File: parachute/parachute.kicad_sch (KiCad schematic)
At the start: 10 parts, among them J1 HMI, J2 battery, J3 trigger, J4 servo, J6 step_up, U1 Optocoupler_DC_PhotoNPN_AKEC, U2 RP2040

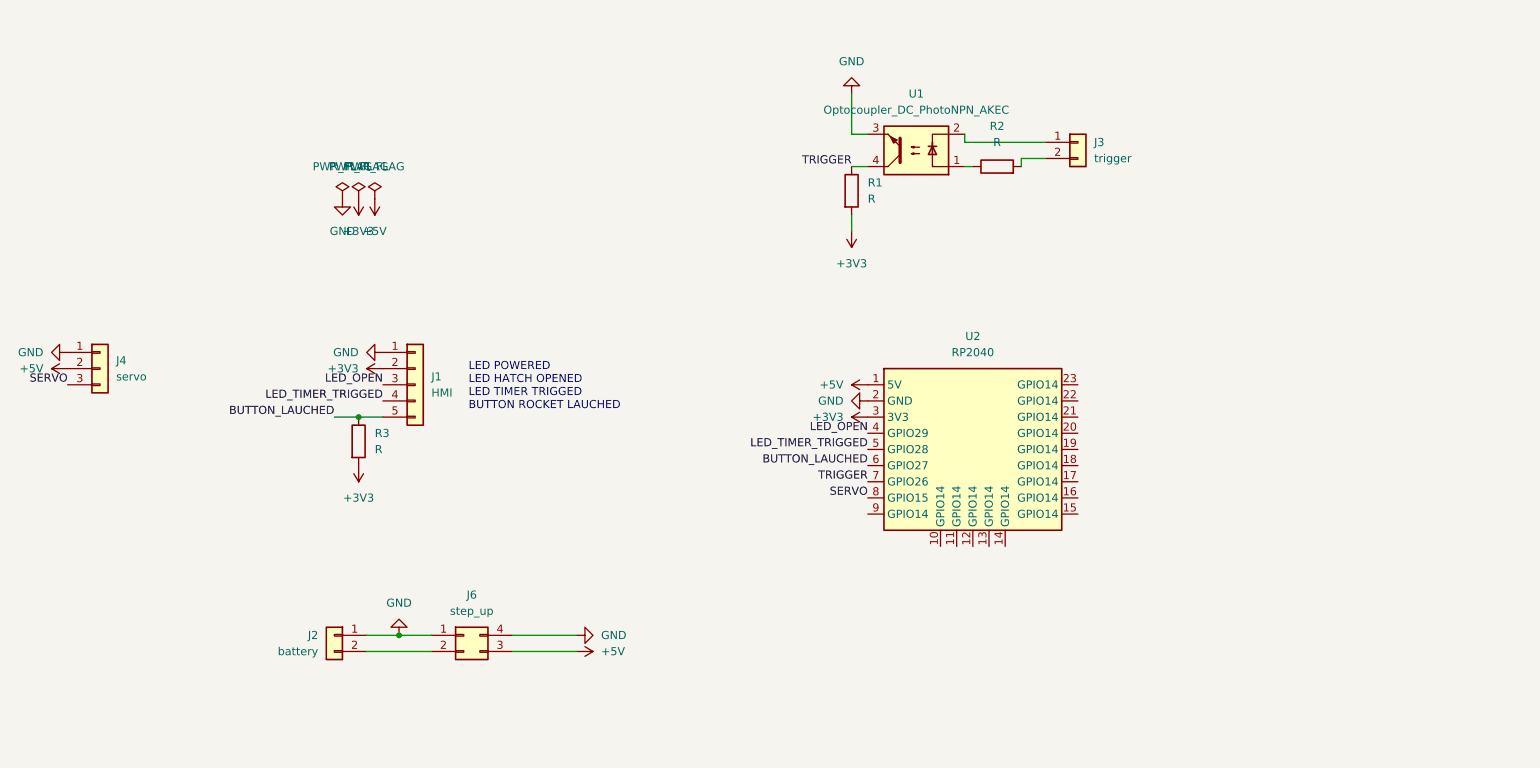
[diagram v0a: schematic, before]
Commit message: ajout d'une carte hmi
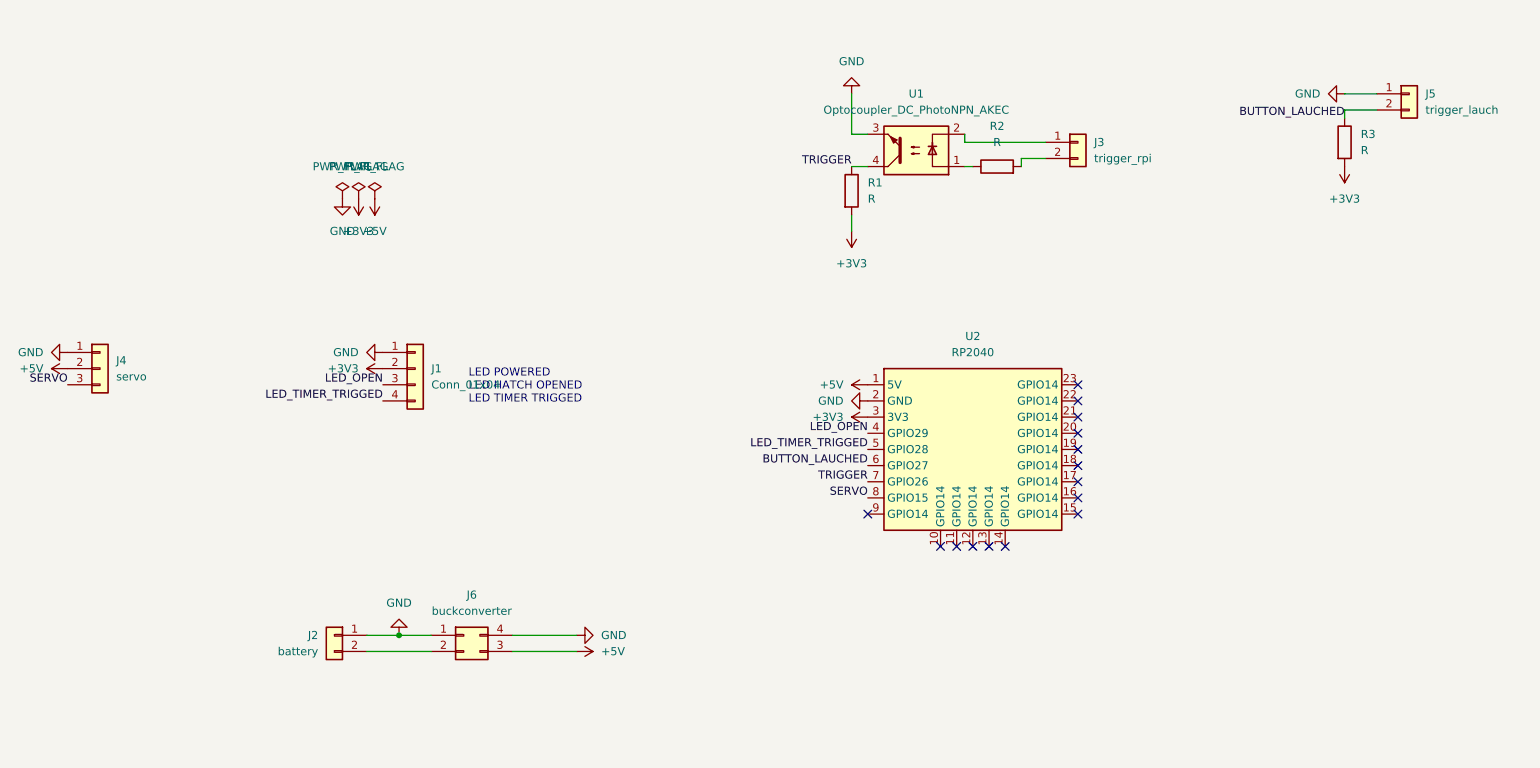
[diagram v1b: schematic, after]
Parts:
- removed J1: HMI, symbol Connector_Generic:Conn_01x05
- added J1: Conn_01x04, symbol Connector_Generic:Conn_01x04
- added J5: trigger_lauch, symbol Connector_Generic:Conn_01x02
- J3: value trigger -> trigger_rpi
- J6: value step_up -> buckconverter
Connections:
- net +3V3: now also J1.2 (Pin_2)
- net BUTTON_LAUCHED: now also J5.2 (Pin_2)
- net GND: now also J1.1 (Pin_1), J5.1 (Pin_1)
- net LED_OPEN: now also J1.3 (Pin_3)
- net LED_TIMER_TRIGGED: now also J1.4 (Pin_4)
- no-connect marks 0 -> 15
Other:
- note added: "LED POWERED LED HATCH OPENED LED TIMER TRIGGED"
- note removed: "LED POWERED LED HATCH OPENED LED TIMER TRIGGED BUTTON ROCKET LAUCHED"
- moved on the sheet: R3

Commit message: update parachute to have back information
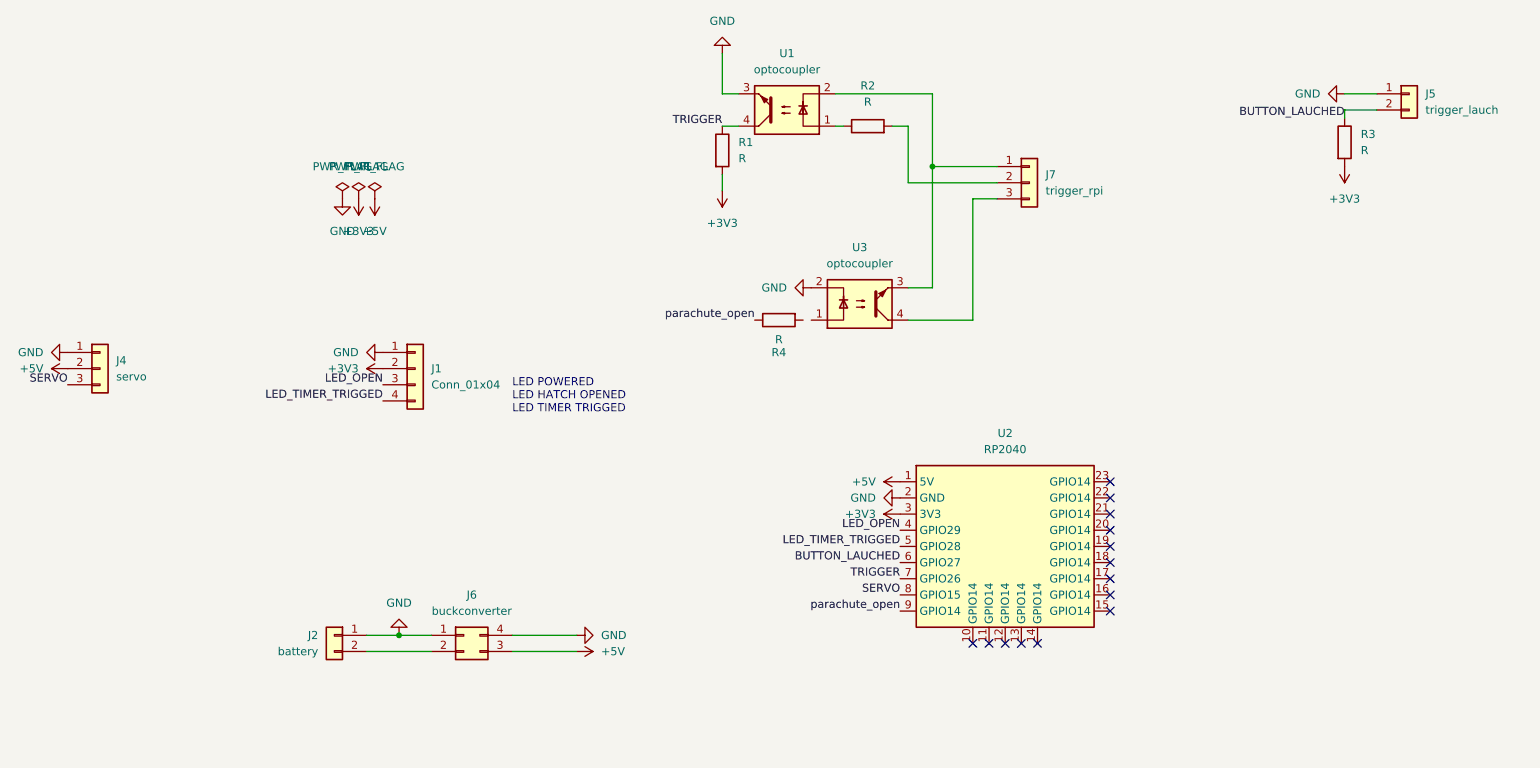
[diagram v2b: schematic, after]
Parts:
- removed J3: trigger_rpi, symbol Connector_Generic:Conn_01x02
- added J7: trigger_rpi, symbol Connector_Generic:Conn_01x03
- added R4: R, symbol Device:R
- added U3: optocoupler, symbol Isolator:Optocoupler_DC_PhotoNPN_AKEC
- U1: value Optocoupler_DC_PhotoNPN_AKEC -> optocoupler
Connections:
- net GND: now also U3.2
- net parachute_open: now reaches U2.9 (GPIO14)
- net parachute_open: now also R4.1
- net at U1.2: now also J7.1 (Pin_1), U3.3
- net at R2.2: now also J7.2 (Pin_2)
- new net: J7.3 (Pin_3), U3.4
- no-connect marks 15 -> 14
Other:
- moved on the sheet: R1, R2, U1, U2

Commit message: mise à jour du circuit du parachute, début de la création de la carte PCB
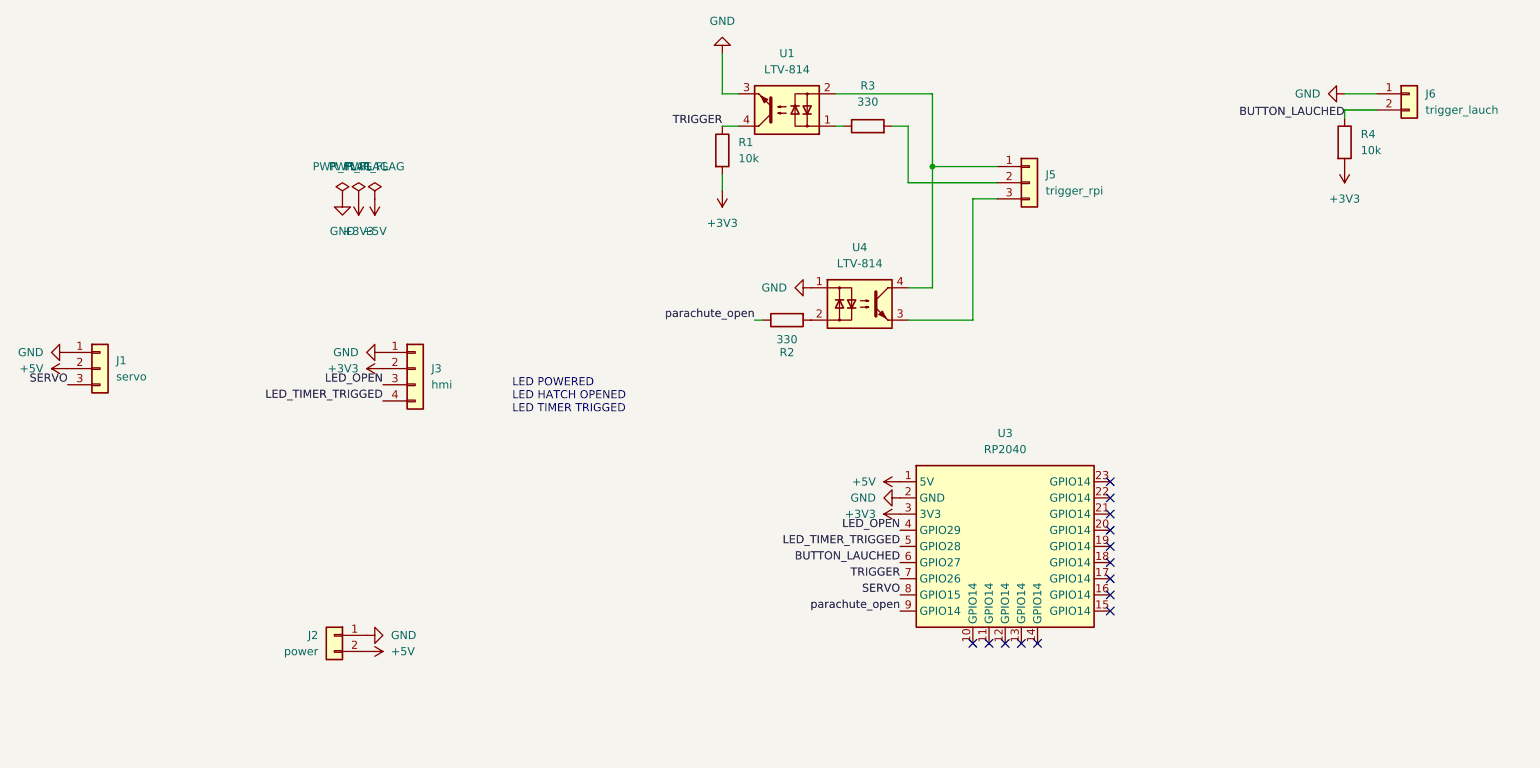
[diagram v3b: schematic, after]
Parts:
- removed J6: buckconverter, symbol Connector_Generic:Conn_02x02_Counter_Clockwise
- removed U1, U3: optocoupler, symbol Isolator:Optocoupler_DC_PhotoNPN_AKEC
- added U1, U4: LTV-814, Package_DIP:DIP-4_W7.62mm, symbol Isolator:LTV-814
- J1: renamed from J4; footprint (none) -> Connector_PinHeader_2.54mm:PinHeader_1x03_P2.54mm_Horizontal
- J2: value battery -> power; footprint (none) -> Connector_JST:JST_XH_B2B-XH-A_1x02_P2.50mm_Vertical
- J3: renamed from J1; value Conn_01x04 -> hmi; footprint (none) -> Connector_JST:JST_XH_B4B-XH-A_1x04_P2.50mm_Vertical
- J5: renamed from J7; footprint (none) -> Connector_JST:JST_XH_B3B-XH-A_1x03_P2.50mm_Vertical
- J6: renamed from J5; footprint (none) -> Connector_JST:JST_XH_B2B-XH-A_1x02_P2.50mm_Vertical
- R1: value R -> 10k; footprint (none) -> Resistor_THT:R_Axial_DIN0204_L3.6mm_D1.6mm_P7.62mm_Horizontal
- R2: renamed from R4; value R -> 330; footprint (none) -> Resistor_THT:R_Axial_DIN0204_L3.6mm_D1.6mm_P7.62mm_Horizontal
- R3: renamed from R2; value R -> 330; footprint (none) -> Resistor_THT:R_Axial_DIN0204_L3.6mm_D1.6mm_P7.62mm_Horizontal
- R4: renamed from R3; value R -> 10k; footprint (none) -> Resistor_THT:R_Axial_DIN0204_L3.6mm_D1.6mm_P7.62mm_Horizontal
- renumbered U2 to U3
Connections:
- net +5V: now also J2.2 (Pin_2)
- net GND: now also U1.3, U4.1
- net TRIGGER: now also U1.4
- net at R3.1: now also U1.1
- net at J5.1 (Pin_1): now also U1.2, U4.4
- net at R2.2: now also U4.2
- net at J5.3 (Pin_3): now also U4.3
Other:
- moved on the sheet: R2

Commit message: agencement et piste cuivre pour PCB parachute
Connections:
- net LED_OPEN: now also U3.18 (GPIO5); no longer U3.4 (GPIO29)
- net LED_TIMER_TRIGGED: now also U3.17 (GPIO6); no longer U3.5 (GPIO28)
- net SERVO: now also U3.19 (GPIO4); no longer U3.8 (GPIO15)
- net TRIGGER: now also U3.14 (GPIO9); no longer U3.7 (GPIO26)
- net parachute_open: now also U3.8 (GPIO15); no longer U3.9 (GPIO14)
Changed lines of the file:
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@@
-	)
-	(no_connect
-		(at 195.58 110.49)
 	)
 	(no_connect
@@
 	)
 	(no_connect
+		(at 162.56 105.41)
+	)
+	(no_connect
+		(at 162.56 102.87)
+	)
+	(no_connect
 		(at 195.58 115.57)
 	)
 	(no_connect
-		(at 195.58 107.95)
-	)
-	(no_connect
 		(at 195.58 102.87)
 	)
@@
 	)
 	(no_connect
-		(at 195.58 105.41)
+		(at 162.56 110.49)
+	)
+	(no_connect
+		(at 162.56 115.57)
 	)
 	(no_connect
 		(at 181.61 120.65)
-	)
-	(no_connect
-		(at 184.15 120.65)
 	)
 	(wire
@@
 	)
 	(label "TRIGGER"
-		(at 162.56 110.49 180)
+		(at 184.15 120.65 270)
 		(effects
 			(font
@@
 	)
 	(label "LED_OPEN"
-		(at 162.56 102.87 180)
-		(effects
-			(font
-				(size 1.27 1.27)
-			)
-			(justify right bottom)
+		(at 195.58 107.95 0)
+		(effects
+			(font
+				(size 1.27 1.27)
+			)
+			(justify left bottom)
 		)
 	)
 	(label "LED_TIMER_TRIGGED"
-		(at 162.56 105.41 180)
-		(effects
-			(font
-				(size 1.27 1.27)
-			)
-			(justify right bottom)
+		(at 195.58 110.49 0)
+		(effects
+			(font
+				(size 1.27 1.27)
+			)
+			(justify left bottom)
 		)
 	)
@@
 	)
 	(label "SERVO"
+		(at 195.58 105.41 0)
+		(effects
+			(font
+				(size 1.27 1.27)
+			)
+			(justify left bottom)
+		)
+	)
+	(label "parachute_open"
 		(at 162.56 113.03 180)
 		(effects
 			(font
-				(size 1.27 1.27)
-			)
-			(justify right bottom)
-		)
-	)
-	(label "parachute_open"
-		(at 162.56 115.57 180)
-		(effects
-			(font

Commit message: parachute full revision
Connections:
- net GND: now also U4.2; no longer U4.1
- net parachute_open: now also U3.10 (GPIO13); no longer U3.8 (GPIO15)
- net at R2.2: now also U4.1; no longer U4.2
- net at J5.1 (Pin_1), U1.2: now also U4.3; no longer U4.4
- net at J5.3 (Pin_3): now also U4.4; no longer U4.3
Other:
- moved on the sheet: R2
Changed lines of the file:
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@@
 	)
 	(junction
-		(at 167.64 45.72)
+		(at 173.99 45.72)
 		(diameter 0)
 		(color 0 0 0 0)
@@
 	)
 	(no_connect
-		(at 173.99 120.65)
+		(at 162.56 113.03)
 	)
 	(no_connect
@@
 	(wire
 		(pts
-			(xy 167.64 45.72) (xy 167.64 34.29)
+			(xy 173.99 45.72) (xy 173.99 34.29)
 		)
 		(stroke
@@
 	(wire
 		(pts
+			(xy 173.99 45.72) (xy 177.8 45.72)
+		)
+		(stroke
+			(width 0)
+			(type default)
+		)
+	)
+	(wire
+		(pts
 			(xy 161.29 39.37) (xy 163.83 39.37)
 		)
@@
 	(wire
 		(pts
+			(xy 167.64 64.77) (xy 167.64 50.8)
+		)
+		(stroke
+			(width 0)
+			(type default)
+		)
+	)
+	(wire
+		(pts
 			(xy 232.41 36.83) (xy 232.41 38.1)
 		)
@@
 	(wire
 		(pts
-			(xy 167.64 64.77) (xy 167.64 45.72)
-		)
-		(stroke
-			(width 0)
-			(type default)
-		)
-	)
-	(wire
-		(pts
 			(xy 134.62 46.99) (xy 134.62 49.53)
 		)
@@
 	(wire
 		(pts
-			(xy 167.64 34.29) (xy 152.4 34.29)
-		)
-		(stroke
-			(width 0)
-			(type default)
-		)
-	)
-	(wire
-		(pts
-			(xy 167.64 45.72) (xy 177.8 45.72)
-		)
-		(stroke
-			(width 0)
-			(type default)
-		)
-	)
-	(wire
-		(pts
-			(xy 140.97 69.85) (xy 139.7 69.85)
+			(xy 167.64 50.8) (xy 177.8 50.8)
+		)
+		(stroke
+			(width 0)
+			(type default)
+		)
+	)
+	(wire
+		(pts
+			(xy 173.99 34.29) (xy 152.4 34.29)
 		)
 		(stroke
@@
 	(wire
 		(pts
-			(xy 173.99 69.85) (xy 173.99 50.8)
-		)
-		(stroke
-			(width 0)
-			(type default)
-		)
-	)
-	(wire
-		(pts
-			(xy 173.99 50.8) (xy 177.8 50.8)
-		)
-		(stroke
-			(width 0)
-			(type default)
-		)
-	)
-	(wire
-		(pts
 			(xy 237.49 36.83) (xy 232.41 36.83)
+		)
+		(stroke
+			(width 0)
+			(type default)
+		)
+	)
+	(wire
+		(pts
+			(xy 173.99 45.72) (xy 173.99 69.85)
 		)
 		(stroke
@@
 	)
 	(label "parachute_open"
-		(at 162.56 113.03 180)
+		(at 173.99 120.65 270)
 		(effects
 			(font
@@
 	)
 	(label "parachute_open"
-		(at 139.7 69.85 180)
+		(at 140.97 64.77 180)
 		(effects
 			(font
@@
 	(symbol
 		(lib_id "power:GND")
-		(at 148.59 64.77 270)
+		(at 148.59 69.85 270)
 		(unit 1)
 		(exclude_from_sim no)
@@
 		(fields_autoplaced yes)
 		(property "Reference" "#PWR013"
-			(at 142.24 64.77 0)
+			(at 142.24 69.85 0)
 			(effects
 				(font
@@
 		)
 		(property "Value" "GND"
-			(at 144.78 64.7699 90)
+			(at 144.78 69.8499 90)
 			(effects
 				(font
@@
 		)
 		(property "Footprint" ""
-			(at 148.59 64.77 0)
+			(at 148.59 69.85 0)
 			(effects
 				(font
@@
 		)
 		(property "Datasheet" ""
-			(at 148.59 64.77 0)
+			(at 148.59 69.85 0)
 			(effects
 				(font
@@
 		)
 		(property "Description" "Power symbol creates a global label with name \"GND\" , ground"
-			(at 148.59 64.77 0)
+			(at 148.59 69.85 0)
 			(effects
 				(font
@@
 	(symbol
 		(lib_id "Device:R")
-		(at 144.78 69.85 90)
+		(at 144.78 64.77 90)
 		(mirror x)
 		(unit 1)
@@
 		(dnp no)
 		(property "Reference" "R2"
-			(at 144.78 74.93 90)
+			(at 144.78 69.85 90)
 			(effects
 				(font
@@
 		)
 		(property "Value" "330"
-			(at 144.78 72.898 90)
+			(at 144.78 67.818 90)
 			(effects
 				(font
@@
 		)
 		(property "Footprint" "Resistor_THT:R_Axial_DIN0204_L3.6mm_D1.6mm_P7.62mm_Horizontal"
-			(at 144.78 68.072 90)
+			(at 144.78 62.992 90)
 			(effects
 				(font
@@
 		)
 		(property "Datasheet" "~"
-			(at 144.78 69.85 0)
+			(at 144.78 64.77 0)
 			(effects
 				(font
@@
 		)
 		(property "Description" "Resistor"
-			(at 144.78 69.85 0)
-			(effects
-				(font
+			(at 144.78 64.77 0)
+			(effects
+				(font
